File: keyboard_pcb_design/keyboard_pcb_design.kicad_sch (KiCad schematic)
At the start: 45 parts, among them J1 Conn_01x03, J2 USB4105-GF-A, SW1 Switch, SW2 Switch, SW3 Switch, SW4 Switch, SW5 Switch, SW6 PTS645SH50SMTR92LFS, SW7 PTS645SH50SMTR92LFS, U1 SC09147, U2 NCP1117-3.3_SOT223, U3 MX25L3233FM2I-08Q, U4 SMF05CT1G, X1 ABM8-272-T3

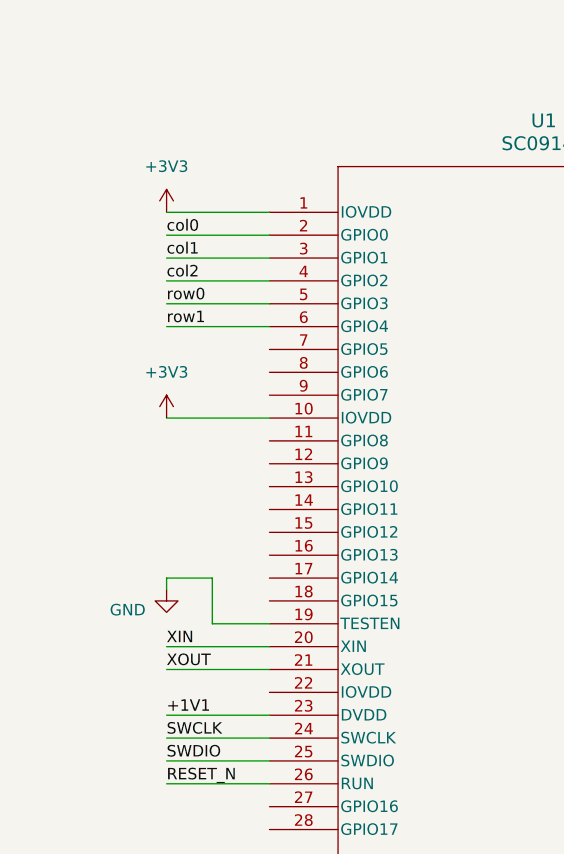
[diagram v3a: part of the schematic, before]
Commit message: fix iovdd connection
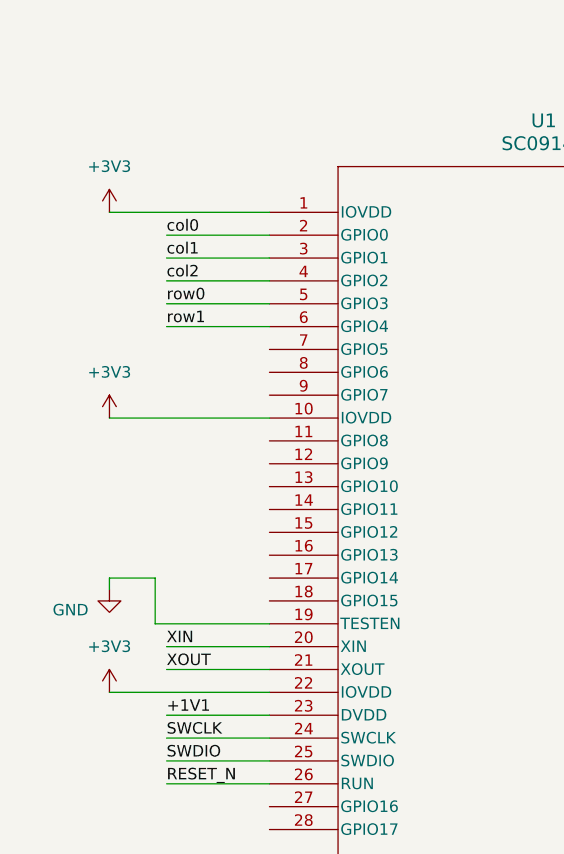
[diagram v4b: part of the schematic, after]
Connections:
- net +3V3: now also U1.22 (IOVDD)
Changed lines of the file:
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@@
 	(wire
 		(pts
-			(xy 30.48 57.15) (xy 41.91 57.15)
+			(xy 24.13 57.15) (xy 41.91 57.15)
 		)
 		(stroke
@@
 	(wire
 		(pts
-			(xy 35.56 80.01) (xy 41.91 80.01)
+			(xy 29.21 80.01) (xy 41.91 80.01)
 		)
 		(stroke
@@
 	(wire
 		(pts
-			(xy 35.56 74.93) (xy 35.56 80.01)
+			(xy 29.21 74.93) (xy 29.21 80.01)
 		)
 		(stroke
@@
 	(wire
 		(pts
-			(xy 30.48 34.29) (xy 41.91 34.29)
+			(xy 24.13 34.29) (xy 41.91 34.29)
 		)
 		(stroke
@@
 	(wire
 		(pts
-			(xy 30.48 74.93) (xy 35.56 74.93)
+			(xy 24.13 74.93) (xy 29.21 74.93)
 		)
 		(stroke
@@
 	(wire
 		(pts
+			(xy 24.13 87.63) (xy 41.91 87.63)
+		)
+		(stroke
+			(width 0)
+			(type default)
+		)
+	)
+	(wire
+		(pts
 			(xy 30.48 39.37) (xy 41.91 39.37)
 		)
@@
 	(wire
 		(pts
-			(xy 30.48 76.2) (xy 30.48 74.93)
+			(xy 24.13 76.2) (xy 24.13 74.93)
 		)
 		(stroke
@@
 	)
 	(symbol
+		(lib_id "power:+3V3")
+		(at 24.13 87.63 0)
+		(unit 1)
+		(exclude_from_sim no)
+		(in_bom yes)
+		(on_board yes)
+		(dnp no)
+		(fields_autoplaced yes)
+		(property "Reference" "#PWR046"
+			(at 24.13 91.44 0)
+			(effects
+				(font
+					(size 1.27 1.27)
+				)
+				(hide yes)
+			)
+		)
+		(property "Value" "+3V3"
+			(at 24.13 82.55 0)
+			(effects
+				(font
+					(size 1.27 1.27)
+				)
+			)
+		)
+		(property "Footprint" ""
+			(at 24.13 87.63 0)
+			(effects
+				(font
+					(size 1.27 1.27)
+				)
+				(hide yes)
+			)
+		)
+		(property "Datasheet" ""
+			(at 24.13 87.63 0)
+			(effects
+				(font
+					(size 1.27 1.27)
+				)
+				(hide yes)
+			)
+		)
+		(property "Description" "Power symbol creates a global label with name \"+3V3\""
+			(at 24.13 87.63 0)
+			(effects
+				(font
+					(size 1.27 1.27)
+				)
+				(hide yes)
+			)
+		)
+		(pin "1"
+		)
+		(instances
+			(project "keyboard_pcb_design"
+				(path "/f9810ab7-9213-4203-bfa9-6536d5a4d26a"
+					(reference "#PWR046")
+					(unit 1)
+				)
+			)
+		)
+	)
+	(symbol
 		(lib_id "Device:C")
 		(at 63.5 184.15 0)
@@
 	(symbol
 		(lib_id "power:+3V3")
-		(at 30.48 57.15 0)
+		(at 24.13 57.15 0)
 		(unit 1)
 		(exclude_from_sim no)
@@
 		(fields_autoplaced yes)
 		(property "Reference" "#PWR011"
-			(at 30.48 60.96 0)
+			(at 24.13 60.96 0)
 			(effects
 				(font
@@
 		)
 		(property "Value" "+3V3"
-			(at 30.48 52.07 0)
+			(at 24.13 52.07 0)
 			(effects
 				(font
@@
 		)
 		(property "Footprint" ""
-			(at 30.48 57.15 0)
+			(at 24.13 57.15 0)
 			(effects
 				(font
@@
 		)
 		(property "Datasheet" ""
-			(at 30.48 57.15 0)
+			(at 24.13 57.15 0)
 			(effects
 				(font
@@
 		)
 		(property "Description" "Power symbol creates a global label with name \"+3V3\""
-			(at 30.48 57.15 0)
+			(at 24.13 57.15 0)
 			(effects
 				(font
@@
 	(symbol
 		(lib_id "power:+3V3")
-		(at 30.48 34.29 0)
+		(at 24.13 34.29 0)
 		(unit 1)
 		(exclude_from_sim no)
@@
 		(fields_autoplaced yes)
 		(property "Reference" "#PWR010"
-			(at 30.48 38.1 0)
+			(at 24.13 38.1 0)
 			(effects
 				(font
@@
 		)
 		(property "Value" "+3V3"
-			(at 30.48 29.21 0)
+			(at 24.13 29.21 0)
 			(effects
 				(font
@@
 		)
 		(property "Footprint" ""
-			(at 30.48 34.29 0)
+			(at 24.13 34.29 0)
 			(effects
 				(font
@@
 		)
 		(property "Datasheet" ""
-			(at 30.48 34.29 0)
+			(at 24.13 34.29 0)
 			(effects
 				(font
@@
 		)
 		(property "Description" "Power symbol creates a global label with name \"+3V3\""
-			(at 30.48 34.29 0)
+			(at 24.13 34.29 0)
 			(effects
 				(font
@@
 	(symbol
 		(lib_id "power:GND")
-		(at 30.48 76.2 0)
+		(at 24.13 76.2 0)
 		(unit 1)
 		(exclude_from_sim no)
@@
 		(dnp no)
 		(property "Reference" "#PWR041"
-			(at 30.48 82.55 0)
+			(at 24.13 82.55 0)
 			(effects
 				(font
@@
 		)
 		(property "Value" "GND"
-			(at 26.162 78.486 0)
+			(at 19.812 78.486 0)
 			(effects
 				(font
@@
 		)
 		(property "Footprint" ""
-			(at 30.48 76.2 0)
+			(at 24.13 76.2 0)
 			(effects
 				(font
@@
 		)
 		(property "Datasheet" ""
-			(at 30.48 76.2 0)
+			(at 24.13 76.2 0)
 			(effects
 				(font
@@
 		)
 		(property "Description" "Power symbol creates a global label with name \"GND\" , ground"
-			(at 30.48 76.2 0)
+			(at 24.13 76.2 0)
 			(effects
 				(font

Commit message: complete joystick schematic
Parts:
- added C18: 0.1u, Capacitor_SMD:C_0201_0603Metric, symbol Device:C
- added R10: 10k, symbol Device:R
- added U5: 1528-5628-ND, symbol keyboard_library:1528-5628-ND
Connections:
- net +3V3: now also C18.1, U5.6 (VCC)
- net GND: now also C18.2, U5.2 (GND), U5.5 (GND)
- net ADC0: now reaches U1.38 (GPIO26/ADC0)
- net ADC0: now also U5.1 (AD1)
- net ADC1: now reaches U1.39 (GPIO27/ADC1)
- net ADC1: now also U5.4 (AD2)
- net joy_switch: now reaches U1.7 (GPIO5)
- net joy_switch: now also R10.1
- new net: R10.2, U5.3 (Switch)
- no-connect marks 3 -> 25
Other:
- note added: "joystick"
- moved on the sheet: C14, C15, C17, C3, C4, R3, R4, R5, R8, R9, SW6, SW7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

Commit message: assign footprints to symbols
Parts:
- C17: footprint (none) -> Capacitor_SMD:C_0201_0603Metric
- J1: footprint (none) -> Connector_PinHeader_2.54mm:PinHeader_1x03_P2.54mm_Horizontal
- R10, R8, R9: footprint (none) -> Resistor_SMD:R_0201_0603Metric
- SW6, SW7: footprint (none) -> keyboard_footprint:PTS645SL50SMTR92 LFS
- U5: footprint (none) -> keyboard_footprint:1528-5628-ND
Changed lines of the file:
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@@
 			)
 		)
-		(property "Footprint" ""
+		(property "Footprint" "keyboard_footprint:1528-5628-ND"
 			(at 25.4 124.46 0)
 			(effects
@@
 			)
 		)
-		(property "Footprint" ""
+		(property "Footprint" "Capacitor_SMD:C_0201_0603Metric"
 			(at 63.1952 187.96 0)
 			(effects
@@
 			)
 		)
-		(property "Footprint" ""
+		(property "Footprint" "Resistor_SMD:R_0201_0603Metric"
 			(at 64.77 125.222 90)
 			(effects
@@
 			)
 		)
-		(property "Footprint" ""
+		(property "Footprint" "Resistor_SMD:R_0201_0603Metric"
 			(at 51.308 170.18 90)
 			(effects
@@
 			)
 		)
-		(property "Footprint" ""
+		(property "Footprint" "Resistor_SMD:R_0201_0603Metric"
 			(at 57.15 180.848 90)
 			(effects
@@
 			)
 		)
-		(property "Footprint" ""
+		(property "Footprint" "keyboard_footprint:PTS645SL50SMTR92 LFS"
 			(at 20.32 179.07 0)
 			(effects
@@
 			)
 		)
-		(property "Footprint" ""
+		(property "Footprint" "Connector_PinHeader_2.54mm:PinHeader_1x03_P2.54mm_Horizontal"
 			(at 181.61 22.86 0)
 			(effects
@@
 			)
 		)
-		(property "Footprint" ""
+		(property "Footprint" "keyboard_footprint:PTS645SL50SMTR92 LFS"
 			(at 100.33 179.07 0)
 			(effects
